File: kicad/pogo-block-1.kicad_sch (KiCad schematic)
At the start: 22 parts, among them J3 ALT_BP_L, J4 ALT_BP_R, SW1 GAIN_MAIN, SW2 GAIN_BP3, U2 OPA1612, U3 OPA1612

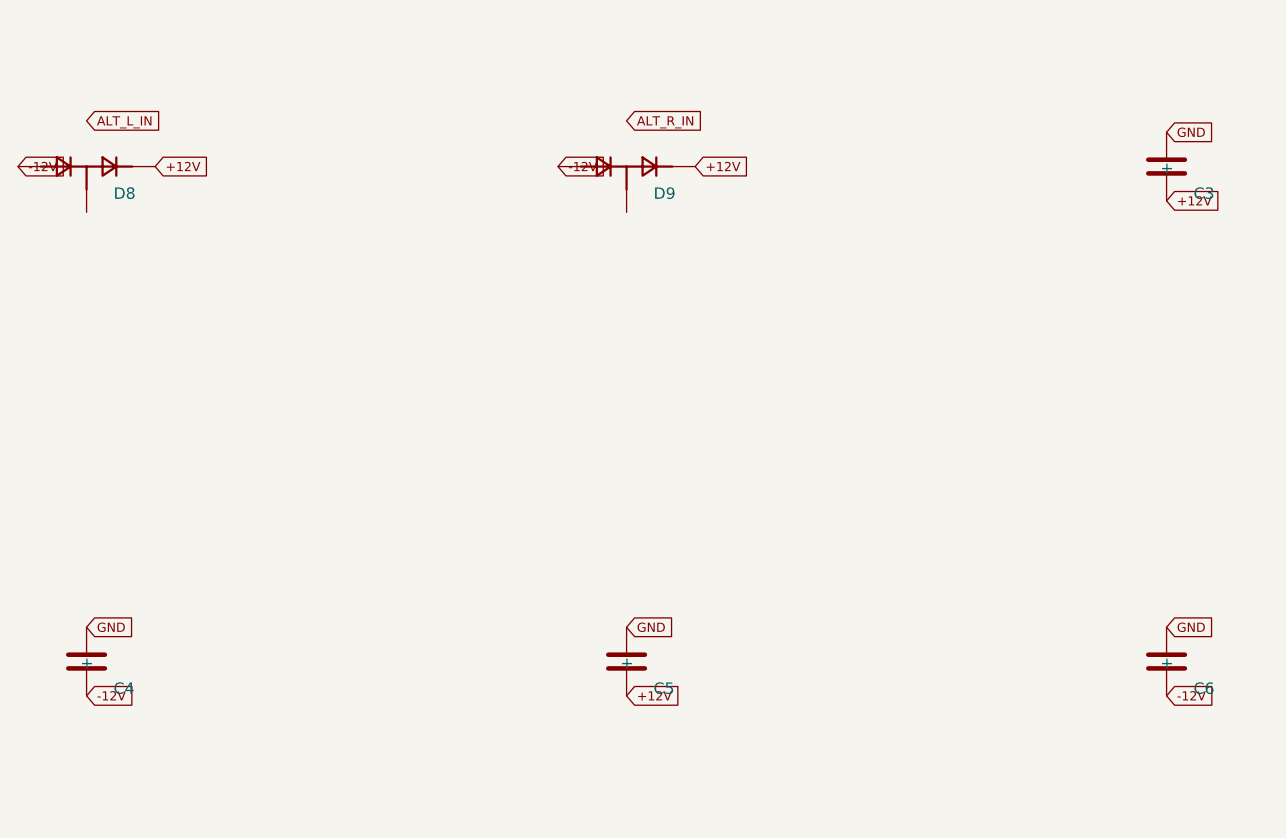
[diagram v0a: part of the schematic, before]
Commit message: 0015-component-audit: apply component verification fixes
Board-breaking:
- that2180: real MPN THAT2180AL08-U (grade A) + package SIP-8 (THT); vendor
  Package_SIP/SIP-8_2.54mm footprint; fix components.yaml U4/U5 + CLAUDE.md.
  The 2180 has no SMD/SOIC variant.
- bat54s: redraw symbol to real series topology (1=A1, 2=K2, 3=K1;A2 junction);
  swap pins 2<->3 on all 24 BAT54S instances (blocks A/1/3/4) so signal sits on the
  junction (pin3), +12V on K2 (pin2), -12V on A1 (pin1); fix aux-cv-protection.md +
  block-A spec (both mislabeled the signal node as pin 2).

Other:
- R_INV_IN/R_INV_FB: add tol 1% (header-required >60 dB null).
- slide_pot_45mm: MPN RA4522F (Alpha 45mm, Rapid/Banzai); fix datasheet link.
- bzx84c10: add shared BZX84_SER datasheet (committed PDF + sha256); canonical MPN.
- opa1612: add symbol opamp2. bourns_3296w/3224w: fix version strings.
- cd4053 symbol doc# -> SCHS047O; c.yaml pin1 '+' -> '~' (non-polarized).

Jack S/T/TN reconciliation deferred (its own change). Plugin DSP untouched.
Regenerated all schematics, BOM, fp-lib-table, footprint SVGs, panel; 5 gates green.
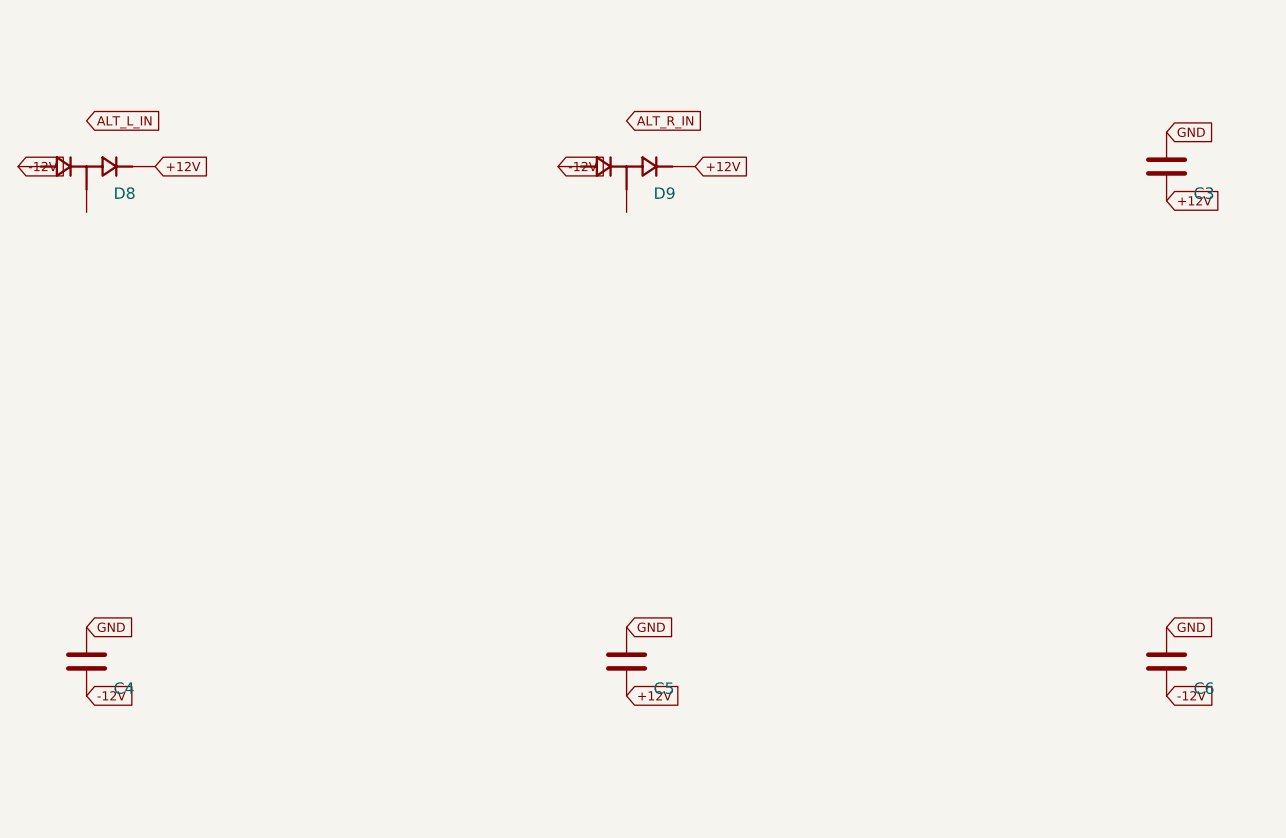
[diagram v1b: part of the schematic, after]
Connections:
- net +12V: now also D8.2 (K2), D9.2 (K2); no longer D8.3 (K2), D9.3 (K2)

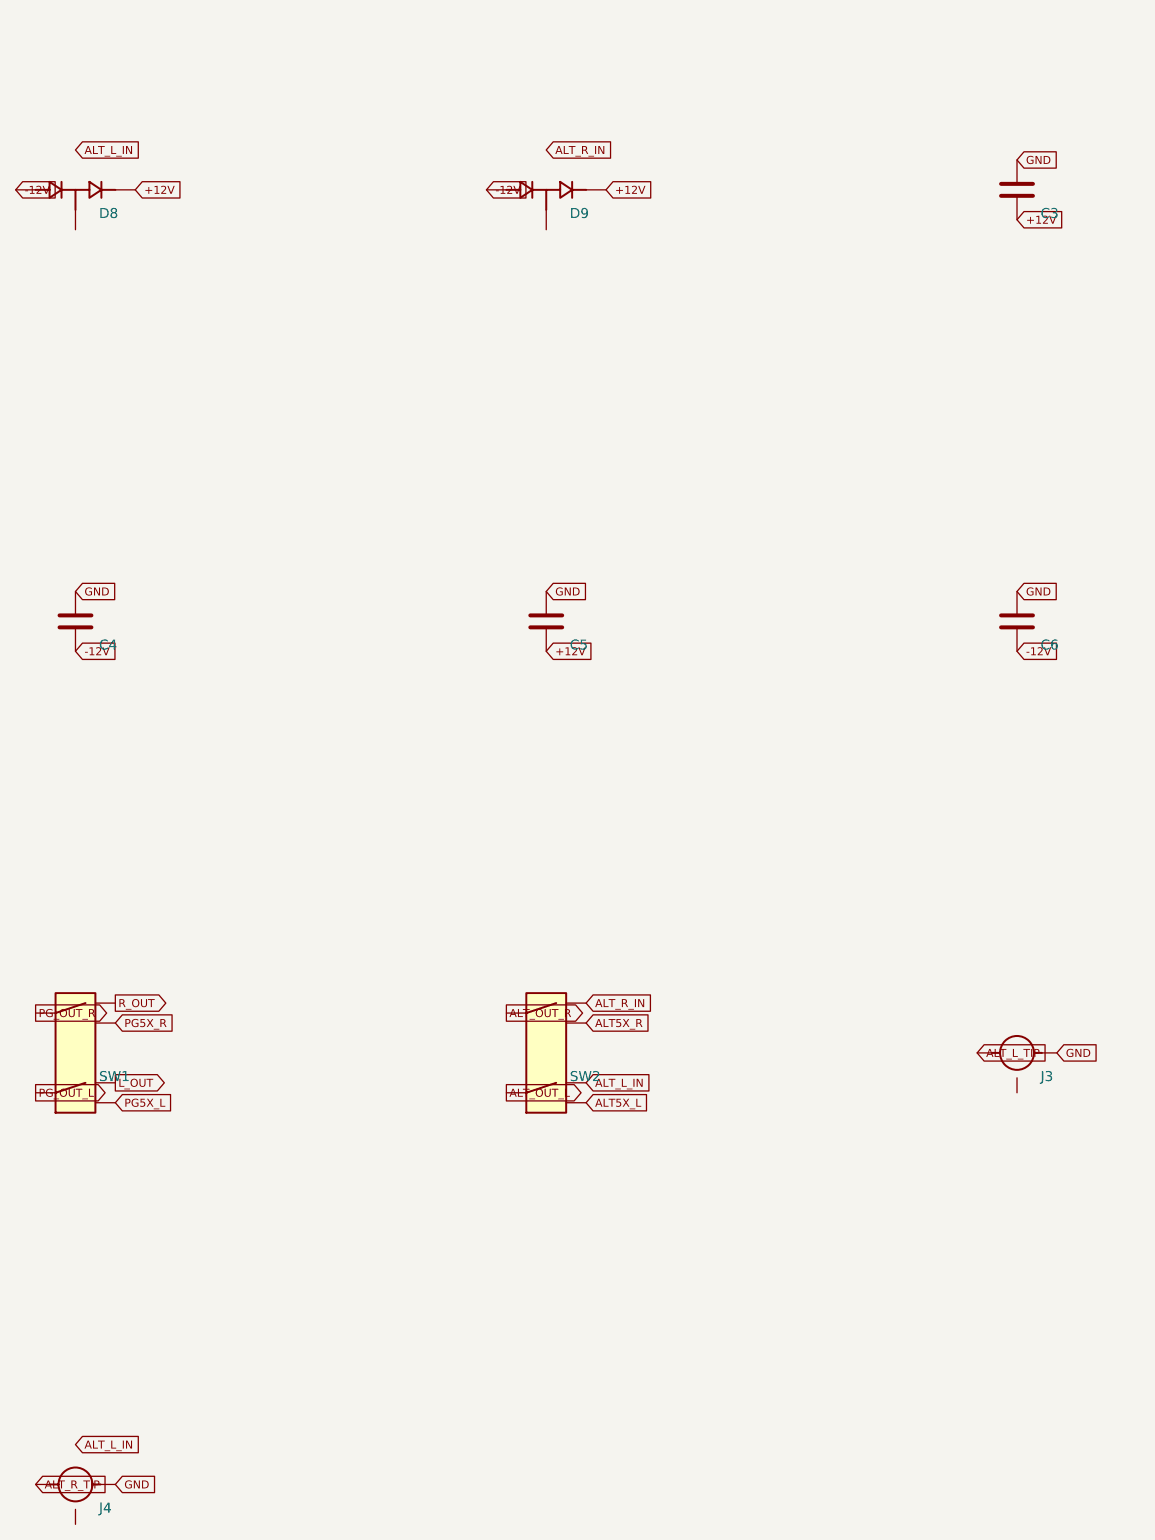
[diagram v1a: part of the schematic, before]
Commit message: 0018: block-6 stage 3 - BP3 input selector (ALT-VCA vs LP1)
Build the BP3 input selector the plugin requires (Pogo.cpp:440-441): a CD4053
mux (U81, block-6-dist3) picks per channel between the LP1 band (LP1_OUT) and
the ALT-VCA voice (block-4 ALT_VCA_OUT), feeding BP3's distortion input.
- Select = ALT_L_DET, an ALT_BP_L insertion detect: J3 tip-switch lug (block-1)
  -> ALT_L_DET, +12V pull-up (R133, dist3) + 22k tip pulldown (R134, block-1);
  patched=ALT-VCA, unpatched=LP1.
- BP3IN is now an internal dist3 net (mux out -> distortion), resolving the
  previously hand-waved boundary. New boundary nets: ALT_L_DET (block-1->dist3),
  ALT_VCA_OUT_L/R (block-4->dist3), LP1_OUT extended to dist3.
- Single ALT_L_DET drives both channels (user decision): the locked single-switch
  jacks leave no free contact for an ALT_R detect (J4's switch is the R-normal),
  so the plugin's asymmetric bp3InR=(L||R) is dropped -- diverges only in the
  rare R-patched-not-L case.

CD4053 selector + components (G5/G6a). All 5 --check gates + parity green;
boundary symmetry verified.

https://claude.ai/code/session_013jFXG5oeMVSYP7iRpwGvtQ
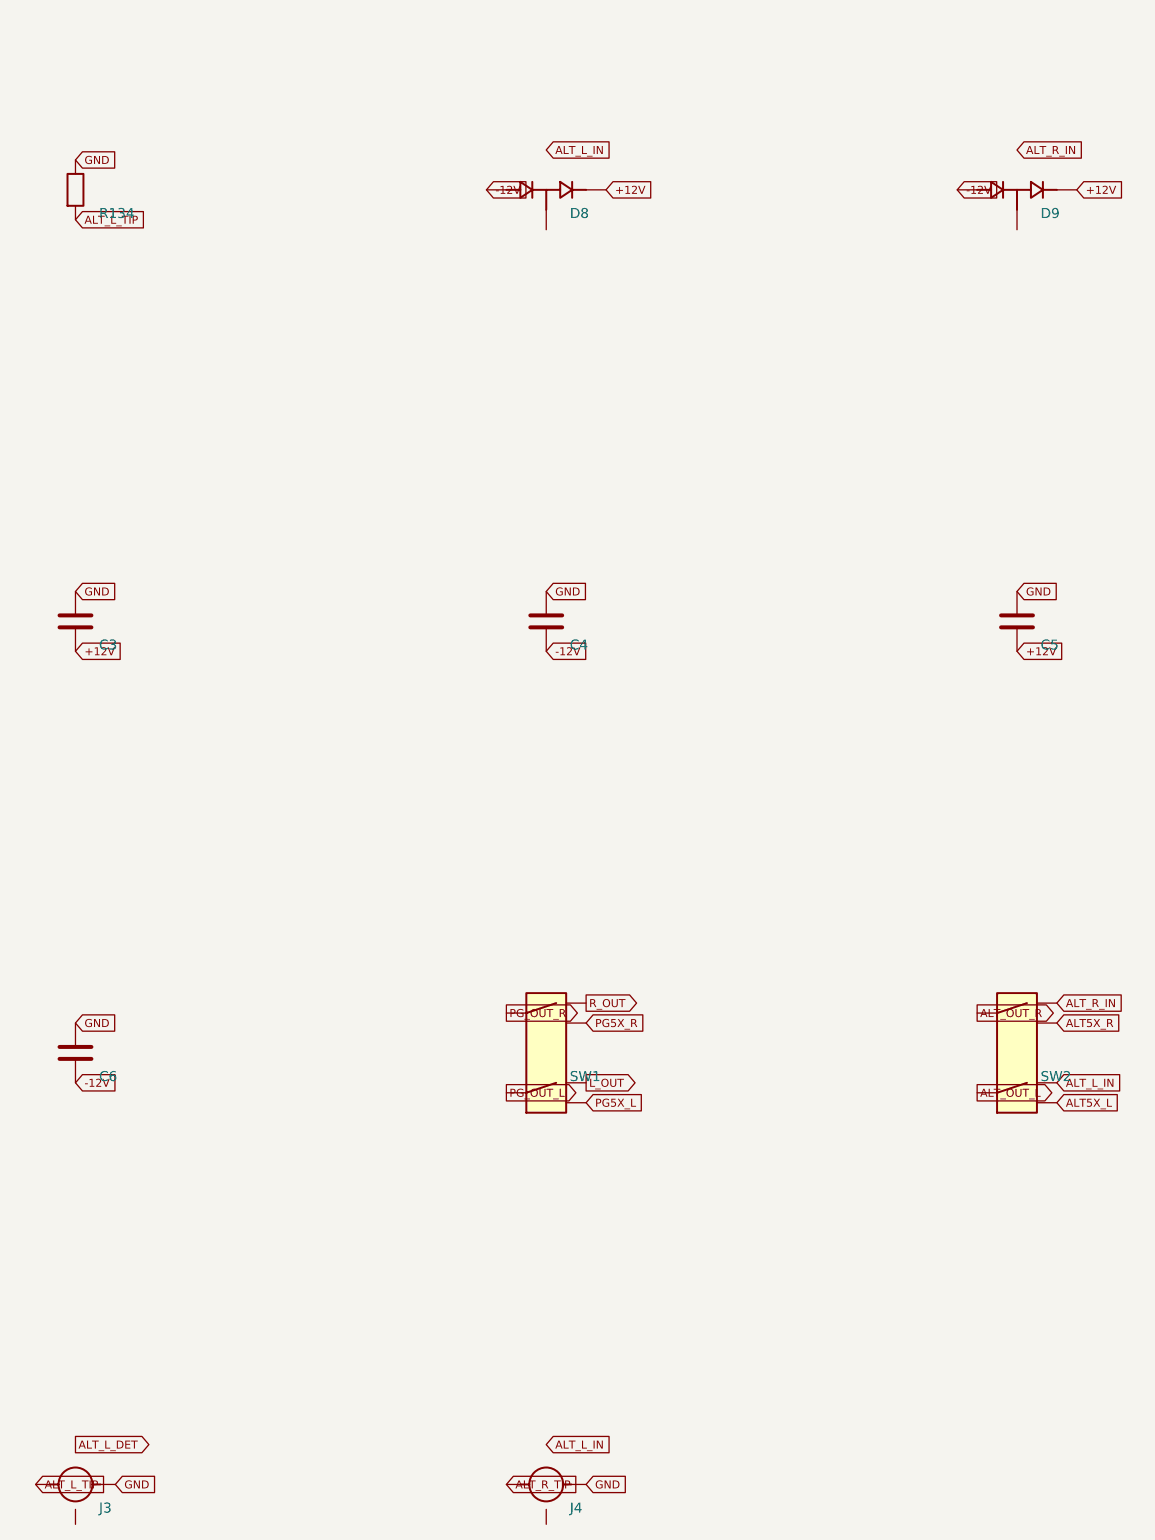
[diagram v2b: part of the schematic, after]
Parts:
- added J4: ALT_BP_R, POGO_Connector_Audio:Jack_3.5mm_QingPu_WQP-PJ398SM_Vertical_CircularHoles, symbol Device:Audio_Jack_3.5mm_SwitchT
- C6: renamed from SW1; value GAIN_MAIN -> 100nF; footprint POGO_Button_Switch_THT:SW_Dailywell_DW3_DPDT -> (none); symbol Switch:SW_Dailywell_DW3 -> Device:C
- D9: renamed from C3; value 100nF -> BAT54S; footprint (none) -> POGO_Package_TO_SOT_SMD:SOT-23; symbol Device:C -> Diode:BAT54S
- J3: renamed from J4; value ALT_BP_R -> ALT_BP_L
- R134: renamed from D8; value BAT54S -> 22k; footprint POGO_Package_TO_SOT_SMD:SOT-23 -> (none); symbol Diode:BAT54S -> Device:R
- SW1: renamed from SW2; value GAIN_BP3 -> GAIN_MAIN
- SW2: renamed from J3; value ALT_BP_L -> GAIN_BP3; footprint POGO_Connector_Audio:Jack_3.5mm_QingPu_WQP-PJ398SM_Vertical_CircularHoles -> POGO_Button_Switch_THT:SW_Dailywell_DW3_DPDT; symbol Device:Audio_Jack_3.5mm_SwitchT -> Switch:SW_Dailywell_DW3
- renumbered C4 to C3, C5 to C4, C6 to C5, D9 to D8
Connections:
- net +12V: now also C3.2, C5.2; no longer C4.2, R134.2 (K2)
- net -12V: now also C4.2, C6.2, D9.1 (A1); no longer C3.2, C5.2, R134.1 (A1)
- net ALT5X_L: now also SW2.6 (B2); no longer SW1.6 (B2)
- net ALT5X_R: now also SW2.3 (A2); no longer SW1.3 (A2)
- net ALT_L_IN: now also SW2.4 (B1); no longer SW1.4 (B1)
- net ALT_L_TIP: now also J3.1 (T), R134.2; no longer SW2.1 (T)
- net ALT_OUT_L: now also SW2.5 (B_COM); no longer SW1.5 (B_COM)
- net ALT_OUT_R: now also SW2.2 (A_COM); no longer SW1.2 (A_COM)
- net ALT_R_IN: now also SW2.1 (A1); no longer SW1.1 (A1)
- net ALT_R_TIP: now also J4.1 (T); no longer J3.1 (T)
- net GND: now also C6.1, R134.1, J4.2 (S); no longer D9.1, SW2.2 (S)
- net L_OUT: now also SW1.4 (B1); no longer C6.4 (B1)
- net PG5X_L: now also SW1.6 (B2); no longer C6.6 (B2)
- net PG5X_R: now also SW1.3 (A2); no longer C6.3 (A2)
- net PG_OUT_L: now also SW1.5 (B_COM); no longer C6.5 (B_COM)
- net PG_OUT_R: now also SW1.2 (A_COM); no longer C6.2 (A_COM)
- net R_OUT: now also SW1.1 (A1); no longer C6.1 (A1)
